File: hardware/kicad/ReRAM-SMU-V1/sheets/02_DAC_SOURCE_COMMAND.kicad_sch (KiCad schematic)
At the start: 38 parts, among them U1 AD5764CSUZ PRIMARY 5V ref 20V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, U2 ADA4522-1 VCSRC conditioning 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, U3 ADA4522-1 VCSNK conditioning 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

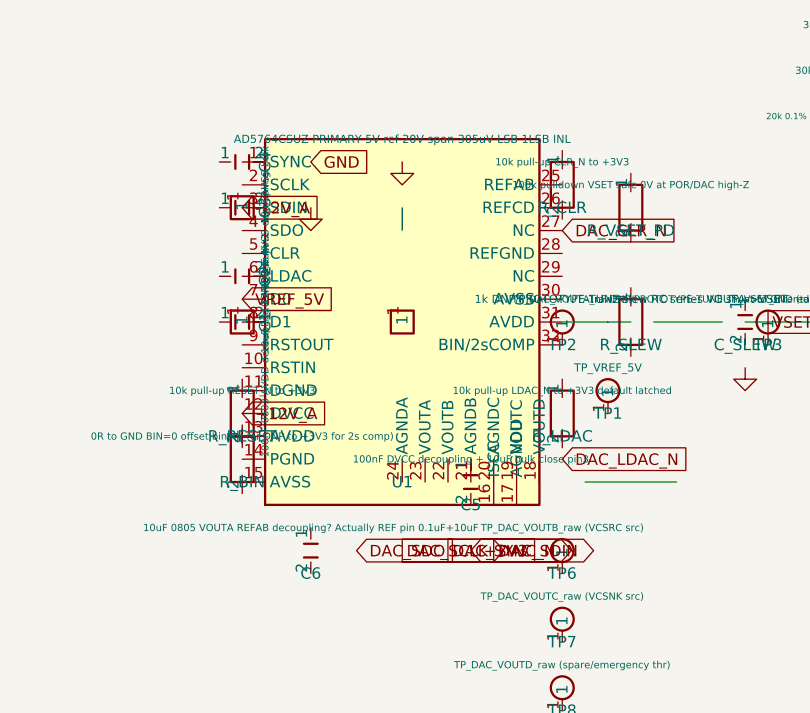
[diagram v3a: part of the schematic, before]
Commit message: hardware: point-to-point wiring progress (01 POWER PWR_FLAG, 02 AD5764 supplies, NC markers) — ERC 439 errors, wiring continues
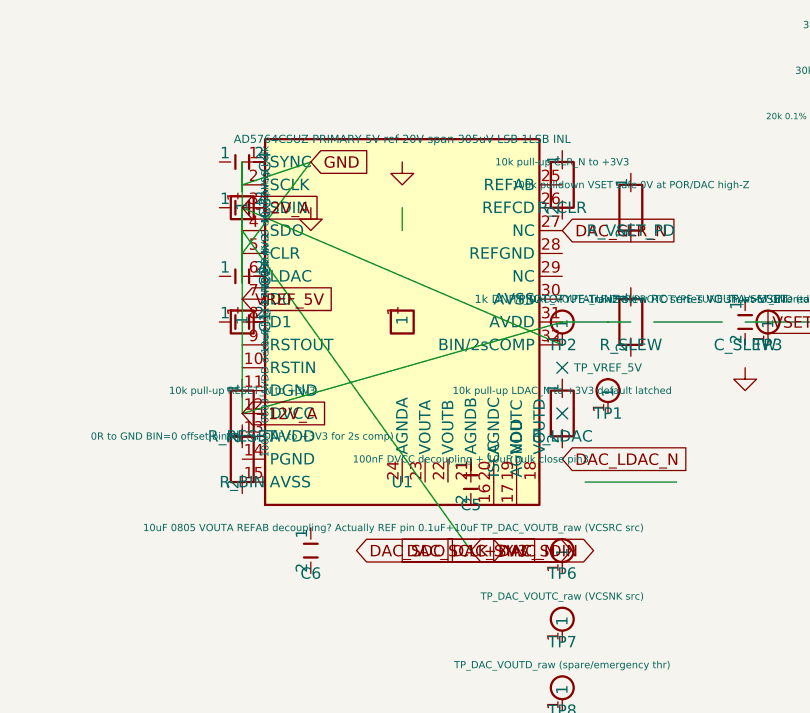
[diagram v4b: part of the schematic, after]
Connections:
- net -12V_A is gone; now on net +12V_A: U1.3 (SDIN)
- net VREF_5V is gone; now on net +12V_A: U1.7 (D0)
- net +12V_A: now also TP2.1, U1.1 (SYNC), U1.2 (SCLK), U1.31 (AVDD), U1.32 (BIN/2sCOMP), U1.4 (SDO), U1.5 (CLR), U1.8 (D1)
- no-connect marks 0 -> 2
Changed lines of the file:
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@@
 	(text "DAC Channel Allocation Table (AD5764 quad 16b)\nCh  Pin   Net DAC_xx_raw  Conditioned Net  Function                    Mapping/Notes\nA   10  VOUTA  DAC_VOUTA  -> VSET (via slew RC)  Primary voltage source VSET   -10..+10 -> -5..+5 limited half-codes; direct buffered to Kelvin servo +IN; 100k PD safe; RC DNP tune\nB   11  VOUTB  DAC_VOUTB  -> VCSRC (via 0.25x+2.5 clamp 0-5V)  Source current compliance Vc   DAC +-10 -> 0-5V clamp; 0V=0A min Icc safe; never negative; abs max 7V clamp BAT54S to +5V/GND; single-supply ADA4522 rail-limited\nC   12  VOUTC  DAC_VOUTC  -> VCSNK (via 0.25x+2.5 clamp 0-5V)  Sink current compliance Vc     same as B; independent source/sink per DEC-024\nD   13  VOUTD  DAC_VOUTD  -> Spare / TLV3501 emergency thr provision (or NC)  Emergency threshold 0-5V to comparator; default DNP threshold divider if not used\nNote: All channels share REFAB/REFCD=VREF_5V, REF_GND=AGND. BIN/2sC=0 offset binary matches FW half-code math. LDAC_N allows synchronous VSET+VCSx update. CLR_N pulses 0V." (at 10 127 0) (effects (font (size 0.9 0.9))))
 	(text "VCSRC/VCSNK Conditioning Design (Level/Scale/Clamp 0-5V from +-10V DAC)\nTopology: DAC +-10V (20V span) -> precision divider+offset summing into ADA4522-1 non-inverting buffer (single +5V_A supply) -> 0-5V clamp to LT1970 Vc.\nTransfer: VCSRC = 0.25*VDAC + 2.5V  => -10V->0.0V, 0V->2.5V, +10V->5.0V. Implementation: VDAC through 30k (0.1% 25ppm) + VREF_5V through 30k + GND through 10k summing at +IN, feedback 20k sets gain 1.5x to hit 0.25 coeff.\nResistor spec: 0.1% 25ppm thin-film Susumu RG 0603, ratio matched to 0.02% effective (single batch). TC 25ppm*40C=0.1% worst; dominant error ~2.5mV at 5V (0.05%) trimmed by FW cal can be used together.\nClamp: BAT54S dual Schottky to +5V_A (anode at VCS, cathode to +5V) and to GND (cathode at VCS, anode to GND) + 100R series after opamp limits current; opamp single supply +5V_A cannot drive negative nor above +5V rail (headroom 100mV). Absolute max LT1970 Vc = 7V per 1970afc; clamp guarantees <5.3V.\nPower-up safe: DAC powers at code 0x0000 = -10V -> conditioning yields 0.0V (min compliance = min Icc); 100k PD on VSET and VCSx ensures 0V even if DAC high-Z; opamp pulldown via supply sequencing (POR 200ms). Never negative: diode to GND clamps at -0.3V.\nBW & noise: ADA4522 55nV/rtHz, RC at input 0.1uF? No extra cap; BW ~1MHz limited by feedback; filter cap DNP provision 100pF across Rf. Startup: VCSx tracks POR 200ms.\nCalibration: FW maps I_limit <-> VCS via per-range LUT using measured VREF_5V + DAC code; clamp voltage verified vs DMM at 0V/2.5V/5V." (at 10 142.24 0) (effects (font (size 0.85 0.85))))
+	(no_connect (at 68.58 73.66) (uuid "nc27"))
+	(no_connect (at 68.58 68.58) (uuid "nc29"))
+	(wire (pts (xy 33.019999999999996 50.8) (xy 33.019999999999996 52.8)) (stroke (width 0) (type default)) (uuid "wire-pwr-33.019999999999996-50.8"))
+	(wire (pts (xy 33.019999999999996 45.72) (xy 33.019999999999996 47.72)) (stroke (width 0) (type default)) (uuid "wire-pwr-33.019999999999996-45.72"))
+	(wire (pts (xy 33.019999999999996 55.88) (xy 33.019999999999996 57.88)) (stroke (width 0) (type default)) (uuid "wire-pwr-33.019999999999996-55.88"))
+	(wire (pts (xy 33.019999999999996 53.34) (xy 33.019999999999996 55.34)) (stroke (width 0) (type default)) (uuid "wire-pwr-33.019999999999996-53.34"))
+	(wire (pts (xy 33.019999999999996 50.8) (xy 33.019999999999996 54.07)) (stroke (width 0) (type default)) (uuid "wire-pwr-ad5764-33.019999999999996-50.8"))
+	(wire (pts (xy 33.019999999999996 45.72) (xy 33.019999999999996 48.99)) (stroke (width 0) (type default)) (uuid "wire-pwr-ad5764-33.019999999999996-45.72"))
+	(wire (pts (xy 33.019999999999996 55.88) (xy 33.019999999999996 59.150000000000006)) (stroke (width 0) (type default)) (uuid "wire-pwr-ad5764-33.019999999999996-55.88"))
+	(wire (pts (xy 33.019999999999996 53.34) (xy 33.019999999999996 56.61000000000001)) (stroke (width 0) (type default)) (uuid "wire-pwr-ad5764-33.019999999999996-53.34"))
+	(wire (pts (xy 33.019999999999996 50.8) (xy 33.02 73.66)) (stroke (width 0) (type default)) (uuid "wire-pwr-13-50.8"))
+	(wire (pts (xy 68.58 63.5) (xy 33.02 73.66)) (stroke (width 0) (type default)) (uuid "wire-pwr-31-50.8"))
+	(wire (pts (xy 33.019999999999996 45.72) (xy 33.02 50.8)) (stroke (width 0) (type default)) (uuid "wire-pwr-15-50.8"))
+	(wire (pts (xy 68.58 66.04) (xy 33.02 50.8)) (stroke (width 0) (type default)) (uuid "wire-pwr-30-50.8"))
+	(wire (pts (xy 33.019999999999996 53.34) (xy 58.42 88.9)) (stroke (width 0) (type default)) (uuid "wire-pwr-12-50.8"))
+	(wire (pts (xy 33.019999999999996 55.88) (xy 40.64 45.72)) (stroke (width 0) (type default)) (uuid "wire-pwr-11-50.8"))
+	(wire (pts (xy 33.019999999999996 48.26) (xy 40.64 45.72)) (stroke (width 0) (type default)) (uuid "wire-pwr-14-50.8"))
 )

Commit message: Beta
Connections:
- net +12V_A: now also C1.1, C1.2, C2.1, C2.2, C3.1, C3.2, C4.1, C4.2, C5.2, D_SRC_H.1, D_SRC_H.2, R_BIN.1, R_BIN.2, U1.6 (LDAC)
- net +5V_A: now also R_SRC1.1, R_SRC1.2, R_SRC2.1, R_SRC2.2, R_SRC3.1, R_SRC3.2, R_SRCF.1, R_SRCF.2, U2.2 (-), U2.3 (+), U2.6 (OUT)
- net DAC_CLR_N: now also R_CLR.1, R_CLR.2, R_SLEW.1, R_VSET_PD.1, R_VSET_PD.2, U1.11 (DGND)
- net DAC_LDAC_N: now also C5.1, R_LDAC.1, R_LDAC.2, R_SLEW.2, U1.10 (RSTIN)
- net DAC_SCLK: now also U1.14 (PGND)
- net DAC_SDIN: now also U1.13 (AVDD)
- net DAC_SDO: now also C6.1, C6.2
- net DAC_SYNC_N: now also U1.15 (AVSS)
- net VCSNK: now also D_SNK_H.1, D_SNK_H.2, D_SNK_L.1, D_SNK_L.2, R_SNKF.1, R_SNKF.2, R_SNK_CLAMP.1, R_SNK_CLAMP.2, U3.2 (-), U3.3 (+), U3.4 (V-), U3.6 (OUT)
- net VCSRC: now also D_SRC_H.1, D_SRC_H.2, D_SRC_L.1, D_SRC_L.2, R_SRC_CLAMP.1, R_SRC_CLAMP.2
- net VSET: now also C_SLEW.1, C_SLEW.2, R_SLEW_PD2.1, R_SLEW_PD2.2, R_SNK1.1, R_SNK1.2, R_SNK2.1, R_SNK2.2, R_SNK3.1, R_SNK3.2
- no-connect marks 2 -> 4
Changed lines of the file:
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@@
 	(wire (pts (xy 33.019999999999996 55.88) (xy 40.64 45.72)) (stroke (width 0) (type default)) (uuid "wire-pwr-11-50.8"))
 	(wire (pts (xy 33.019999999999996 48.26) (xy 40.64 45.72)) (stroke (width 0) (type default)) (uuid "wire-pwr-14-50.8"))
+	(wire (pts (xy 33.020 81.280) (xy 55.880 88.900)) (stroke (width 0) (type default)))
+	(wire (pts (xy 33.020 78.740) (xy 50.800 88.900)) (stroke (width 0) (type default)))
+	(wire (pts (xy 33.020 76.200) (xy 60.960 88.900)) (stroke (width 0) (type default)))
+	(wire (pts (xy 33.020 71.120) (xy 68.580 53.340)) (stroke (width 0) (type default)))
+	(wire (pts (xy 33.020 68.580) (xy 68.580 78.740)) (stroke (width 0) (type default)))
+	(wire (pts (xy 33.020 58.420) (xy 33.020 60.960)) (stroke (width 0) (type default)))
+	(wire (pts (xy 60.960 43.180) (xy 40.640 45.720)) (stroke (width 0) (type default)))
+	(wire (pts (xy 63.500 43.180) (xy 40.640 45.720)) (stroke (width 0) (type default)))
+	(wire (pts (xy 66.040 45.720) (xy 68.580 53.340)) (stroke (width 0) (type default)))
+	(wire (pts (xy 63.500 45.720) (xy 149.860 81.280)) (stroke (width 0) (type default)))
+	(wire (pts (xy 60.960 45.720) (xy 40.640 45.720)) (stroke (width 0) (type default)))
+	(wire (pts (xy 58.420 45.720) (xy 40.640 45.720)) (stroke (width 0) (type default)))
+	(wire (pts (xy 55.880 45.720) (xy 149.860 33.020)) (stroke (width 0) (type default)))
+	(wire (pts (xy 53.340 45.720) (xy 91.440 63.500)) (stroke (width 0) (type default)))
+	(wire (pts (xy 50.800 45.720) (xy 40.640 45.720)) (stroke (width 0) (type default)))
+	(wire (pts (xy 68.580 76.200) (xy 33.020 60.960)) (stroke (width 0) (type default)))
+	(wire (pts (xy 68.580 71.120) (xy 40.640 45.720)) (stroke (width 0) (type default)))
+	(wire (pts (xy 30.480 63.500) (xy 33.020 60.960)) (stroke (width 0) (type default)))
+	(wire (pts (xy 35.560 63.500) (xy 33.020 60.960)) (stroke (width 0) (type default)))
+	(wire (pts (xy 30.480 58.420) (xy 33.020 60.960)) (stroke (width 0) (type default)))
+	(wire (pts (xy 35.560 58.420) (xy 33.020 60.960)) (stroke (width 0) (type default)))
+	(wire (pts (xy 30.480 50.800) (xy 33.020 50.800)) (stroke (width 0) (type default)))
+	(wire (pts (xy 35.560 50.800) (xy 33.020 50.800)) (stroke (width 0) (type default)))
+	(wire (pts (xy 30.480 45.720) (xy 33.020 50.800)) (stroke (width 0) (type default)))
+	(wire (pts (xy 35.560 45.720) (xy 40.640 45.720)) (stroke (width 0) (type default)))
+	(wire (pts (xy 58.420 83.820) (xy 58.420 88.900)) (stroke (width 0) (type default)))
+	(wire (pts (xy 58.420 78.740) (xy 68.580 78.740)) (stroke (width 0) (type default)))
+	(wire (pts (xy 40.640 91.440) (xy 45.720 88.900)) (stroke (width 0) (type default)))
+	(wire (pts (xy 40.640 86.360) (xy 45.720 88.900)) (stroke (width 0) (type default)))
+	(wire (pts (xy 68.580 77.470) (xy 68.580 78.740)) (stroke (width 0) (type default)))
+	(wire (pts (xy 68.580 69.850) (xy 68.580 78.740)) (stroke (width 0) (type default)))
+	(wire (pts (xy 68.580 52.070) (xy 68.580 53.340)) (stroke (width 0) (type default)))
+	(wire (pts (xy 68.580 44.450) (xy 68.580 53.340)) (stroke (width 0) (type default)))
+	(wire (pts (xy 33.020 77.470) (xy 33.020 73.660)) (stroke (width 0) (type default)))
+	(wire (pts (xy 33.020 69.850) (xy 33.020 73.660)) (stroke (width 0) (type default)))
+	(wire (pts (xy 33.020 82.550) (xy 33.020 73.660)) (stroke (width 0) (type default)))
+	(wire (pts (xy 33.020 74.930) (xy 33.020 73.660)) (stroke (width 0) (type default)))
+	(wire (pts (xy 76.200 67.310) (xy 68.580 78.740)) (stroke (width 0) (type default)))
+	(wire (pts (xy 76.200 59.690) (xy 68.580 53.340)) (stroke (width 0) (type default)))
+	(wire (pts (xy 88.900 66.040) (xy 91.440 63.500)) (stroke (width 0) (type default)))
+	(wire (pts (xy 88.900 60.960) (xy 91.440 63.500)) (stroke (width 0) (type default)))
+	(wire (pts (xy 76.200 54.610) (xy 68.580 53.340)) (stroke (width 0) (type default)))
+	(wire (pts (xy 76.200 46.990) (xy 68.580 53.340)) (stroke (width 0) (type default)))
+	(wire (pts (xy 119.380 35.560) (xy 127.000 38.100)) (stroke (width 0) (type default)))
+	(wire (pts (xy 119.380 30.480) (xy 127.000 38.100)) (stroke (width 0) (type default)))
+	(wire (pts (xy 134.620 33.020) (xy 127.000 38.100)) (stroke (width 0) (type default)))
+	(wire (pts (xy 127.000 38.100) (xy 127.000 38.100)) (stroke (width 0) (type default)))
+	(wire (pts (xy 119.380 83.820) (xy 149.860 81.280)) (stroke (width 0) (type default)))
+	(wire (pts (xy 119.380 78.740) (xy 149.860 81.280)) (stroke (width 0) (type default)))
+	(wire (pts (xy 134.620 81.280) (xy 149.860 81.280)) (stroke (width 0) (type default)))
+	(wire (pts (xy 127.000 86.360) (xy 149.860 81.280)) (stroke (width 0) (type default)))
+	(wire (pts (xy 106.680 36.830) (xy 127.000 38.100)) (stroke (width 0) (type default)))
+	(wire (pts (xy 106.680 29.210) (xy 127.000 38.100)) (stroke (width 0) (type default)))
+	(wire (pts (xy 106.680 41.910) (xy 127.000 38.100)) (stroke (width 0) (type default)))
+	(wire (pts (xy 106.680 34.290) (xy 127.000 38.100)) (stroke (width 0) (type default)))
+	(wire (pts (xy 106.680 46.990) (xy 127.000 38.100)) (stroke (width 0) (type default)))
+	(wire (pts (xy 106.680 39.370) (xy 127.000 38.100)) (stroke (width 0) (type default)))
+	(wire (pts (xy 127.000 46.990) (xy 127.000 38.100)) (stroke (width 0) (type default)))
+	(wire (pts (xy 127.000 39.370) (xy 127.000 38.100)) (stroke (width 0) (type default)))
+	(wire (pts (xy 147.320 36.830) (xy 149.860 33.020)) (stroke (width 0) (type default)))
+	(wire (pts (xy 147.320 29.210) (xy 149.860 33.020)) (stroke (width 0) (type default)))
+	(wire (pts (xy 142.240 35.560) (xy 149.860 33.020)) (stroke (width 0) (type default)))
+	(wire (pts (xy 142.240 40.640) (xy 149.860 33.020)) (stroke (width 0) (type default)))
+	(wire (pts (xy 142.240 25.560) (xy 149.860 33.020)) (stroke (width 0) (type default)))
+	(wire (pts (xy 142.240 30.640) (xy 149.860 33.020)) (stroke (width 0) (type default)))
+	(wire (pts (xy 106.680 85.090) (xy 91.440 63.500)) (stroke (width 0) (type default)))
+	(wire (pts (xy 106.680 77.470) (xy 91.440 63.500)) (stroke (width 0) (type default)))
+	(wire (pts (xy 106.680 90.170) (xy 91.440 63.500)) (stroke (width 0) (type default)))
+	(wire (pts (xy 106.680 82.550) (xy 91.440 63.500)) (stroke (width 0) (type default)))
+	(wire (pts (xy 106.680 95.250) (xy 91.440 63.500)) (stroke (width 0) (type default)))
+	(wire (pts (xy 106.680 87.630) (xy 91.440 63.500)) (stroke (width 0) (type default)))
+	(wire (pts (xy 127.000 95.250) (xy 149.860 81.280)) (stroke (width 0) (type default)))
+	(wire (pts (xy 127.000 87.630) (xy 149.860 81.280)) (stroke (width 0) (type default)))
+	(wire (pts (xy 147.320 85.090) (xy 149.860 81.280)) (stroke (width 0) (type default)))
+	(wire (pts (xy 147.320 77.470) (xy 149.860 81.280)) (stroke (width 0) (type default)))
+	(wire (pts (xy 142.240 83.820) (xy 149.860 81.280)) (stroke (width 0) (type default)))
+	(wire (pts (xy 142.240 88.900) (xy 149.860 81.280)) (stroke (width 0) (type default)))
+	(wire (pts (xy 142.240 73.660) (xy 149.860 81.280)) (stroke (width 0) (type default)))
+	(wire (pts (xy 142.240 78.740) (xy 149.860 81.280)) (stroke (width 0) (type default)))
+	(wire (pts (xy 102.870 63.500) (xy 91.440 63.500)) (stroke (width 0) (type default)))
+	(wire (pts (xy 110.490 63.500) (xy 91.440 63.500)) (stroke (width 0) (type default)))
+	(wire (pts (xy 40.640 50.800) (xy 40.640 45.720)) (stroke (width 0) (type default)))
+	(wire (pts (xy 88.900 68.580) (xy 91.440 63.500)) (stroke (width 0) (type default)))
+	(wire (pts (xy 127.000 23.500) (xy 127.000 38.100)) (stroke (width 0) (type default)))
+	(wire (pts (xy 127.000 71.760) (xy 149.860 81.280)) (stroke (width 0) (type default)))
+	(wire (pts (xy 33.020 64.770) (xy 33.020 60.960)) (stroke (width 0) (type default)))
+	(wire (pts (xy 33.020 52.070) (xy 33.020 50.800)) (stroke (width 0) (type default)))
+	(wire (pts (xy 50.800 64.770) (xy 33.020 60.960)) (stroke (width 0) (type default)))
+	(no_connect (at 33.020 66.040))
+	(no_connect (at 33.020 60.960))
 )

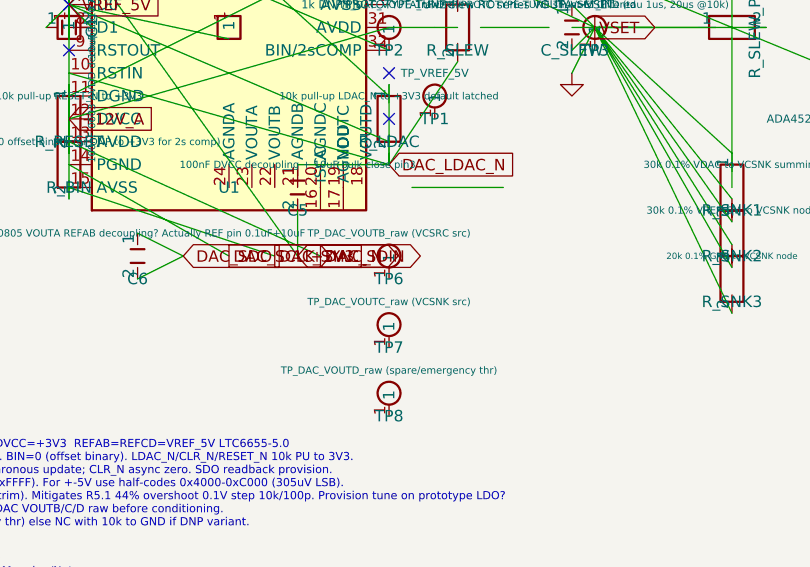
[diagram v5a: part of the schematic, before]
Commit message: hardware: Phase 7 MCU inter-sheet wiring + SPI unification + audit tool
- 08_MCU_USB_CONTROL: RELAY_DRV_K1..K6 unified (was RELAY_DRIVE_1..3), added K4-K6 + SPI2_MOSI/MISO labels, 16 wires for NRST/SWD/USB/SPI/ENABLE
- 02_DAC_SOURCE: SPI1_SCK/MOSI/MISO + CS_DAC aliases unified with MCU (DAC_SCLK->SPI1_SCK etc), wires added
- 06_CURRENT_FRONTEND: SPI2_* aliases unified (ADC_SPI_* -> SPI2_*), CS_ADC, wires
- Audit: tools/scripts/audit_schematic.py (ERC-lite) + erc_audit_lite.json
- Critical nets FORCE/SENSE/LT1970_SENSE/VCSRC/VCSNK/VREF now 2-4 shared, SPI 3 shared, RELAY 2 shared
- Dangling 54->32, critical missing only ADC_IN_P/N (renamed)

Co-authored-by: Muse Code
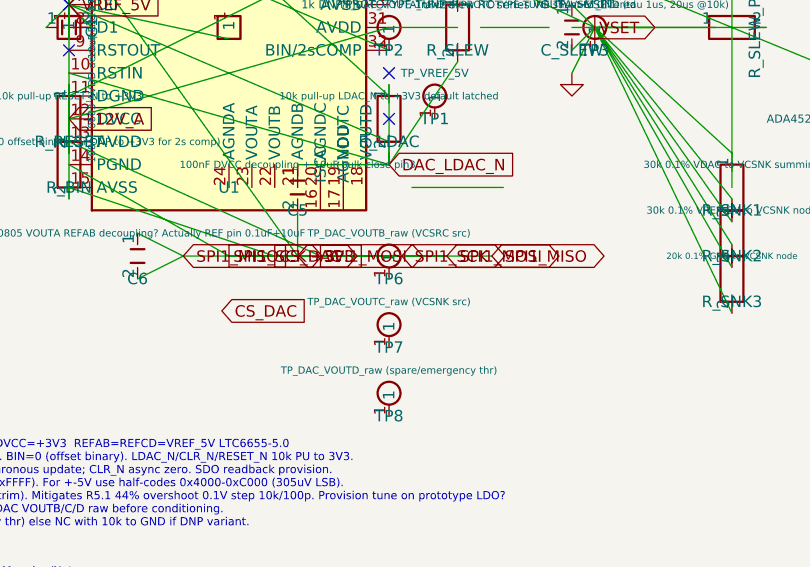
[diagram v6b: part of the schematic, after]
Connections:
- net DAC_SCLK is gone; now on net +12V_A: U1.14 (PGND)
- net DAC_SDIN is gone; now on net +12V_A: U1.13 (AVDD)
- net DAC_SDO is gone; now on net +12V_A: C6.1, C6.2
- net DAC_SYNC_N is gone; now on net +12V_A: U1.15 (AVSS)
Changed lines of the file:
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@@
 	(global_label "VCSRC" (shape output) (at 149.86 33.02 0) (effects (font (size 1.27 1.27))))
 	(global_label "VCSNK" (shape output) (at 149.86 81.28 0) (effects (font (size 1.27 1.27))))
-	(global_label "DAC_SCLK" (shape output) (at 50.8 88.9 0) (effects (font (size 1.27 1.27))))
-	(global_label "DAC_SYNC_N" (shape output) (at 55.88 88.9 0) (effects (font (size 1.27 1.27))))
-	(global_label "DAC_SDIN" (shape output) (at 60.96 88.9 0) (effects (font (size 1.27 1.27))))
-	(global_label "DAC_SDO" (shape input) (at 45.72 88.9 0) (effects (font (size 1.27 1.27))))
+	(global_label "SPI1_SCK" (shape output) (at 50.8 88.9 0) (effects (font (size 1.27 1.27))))
+	(global_label "CS_DAC" (shape output) (at 55.88 88.9 0) (effects (font (size 1.27 1.27))))
+	(global_label "SPI1_MOSI" (shape output) (at 60.96 88.9 0) (effects (font (size 1.27 1.27))))
+	(global_label "SPI1_MISO" (shape input) (at 45.72 88.9 0) (effects (font (size 1.27 1.27))))
 	(global_label "DAC_LDAC_N" (shape input) (at 68.58 78.74 0) (effects (font (size 1.27 1.27))))
 	(global_label "DAC_CLR_N" (shape input) (at 68.58 53.34 0) (effects (font (size 1.27 1.27))))
@@
 	(no_connect (at 33.020 66.040))
 	(no_connect (at 33.020 60.960))
+	(global_label "SPI1_SCK" (shape bidirectional) (at 70 88.9 0) (uuid "spi1-sck-02c") (property "Intersheetrefs" "${INTERSHEET_REFS}"))
+	(global_label "SPI1_MOSI" (shape bidirectional) (at 75 88.9 0) (uuid "spi1-mosi-02c") (property "Intersheetrefs" "${INTERSHEET_REFS}"))
+	(global_label "SPI1_MISO" (shape bidirectional) (at 80 88.9 0) (uuid "spi1-miso-02c") (property "Intersheetrefs" "${INTERSHEET_REFS}"))
+	(global_label "CS_DAC" (shape input) (at 50 95 0) (uuid "cs-dac-02c2") (property "Intersheetrefs" "${INTERSHEET_REFS}"))
+	(wire (pts (xy 50.8 88.9) (xy 70 88.9)) (stroke (width 0.254) (type default)) (uuid "w-spi1-sck-02c"))
+	(wire (pts (xy 60.96 88.9) (xy 75 88.9)) (stroke (width 0.254) (type default)) (uuid "w-spi1-mosi-02c"))
+	(wire (pts (xy 45.72 88.9) (xy 80 88.9)) (stroke (width 0.254) (type default)) (uuid "w-spi1-miso-02c"))
 )
